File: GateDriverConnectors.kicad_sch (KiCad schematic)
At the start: 4 parts, among them J10 PWR/SIG_L1, J12 PWR/SIG_L1, J13 PWR/SIG_H1, J14 GateDriverConn1

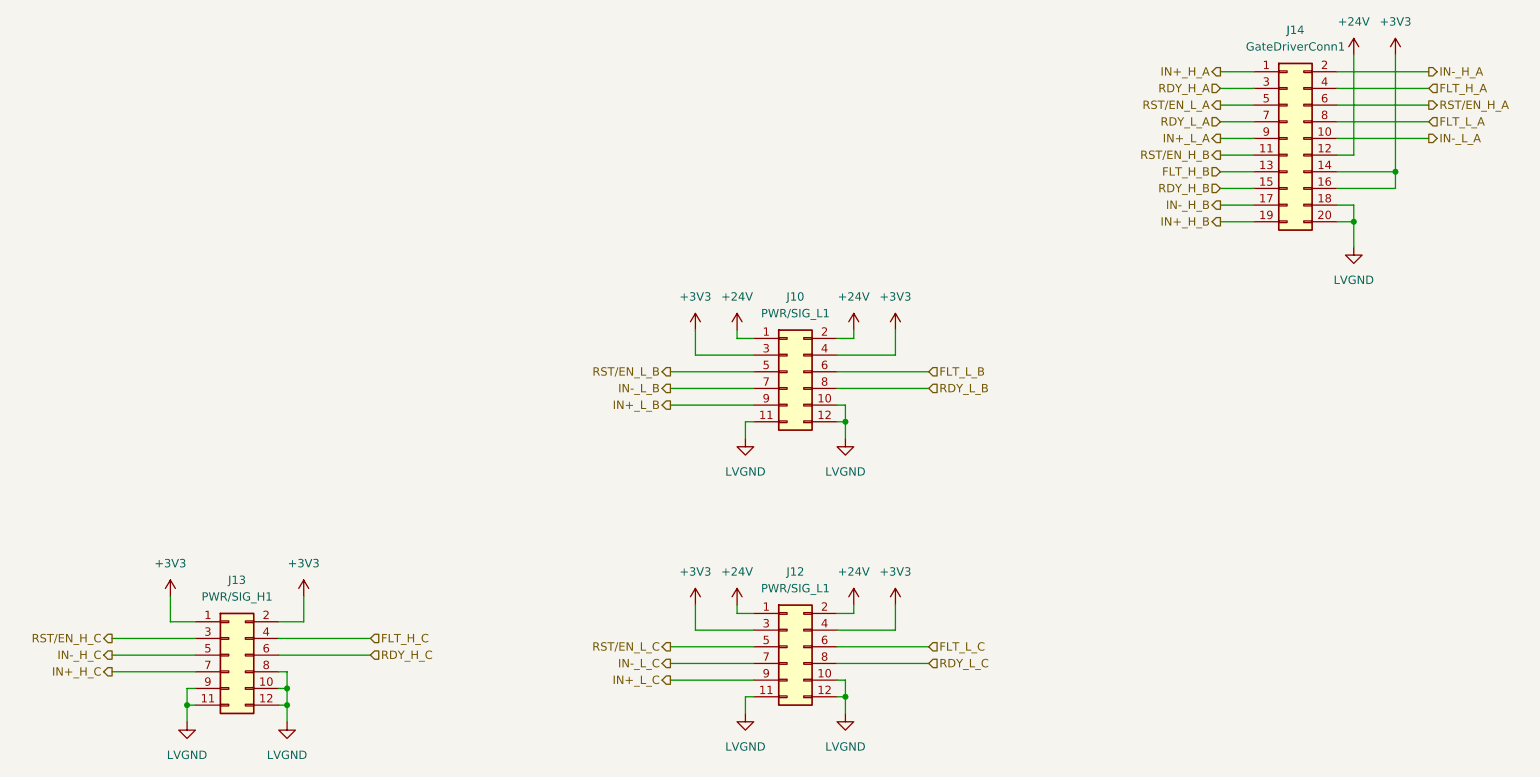
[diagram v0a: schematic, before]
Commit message: gate driver connector 2
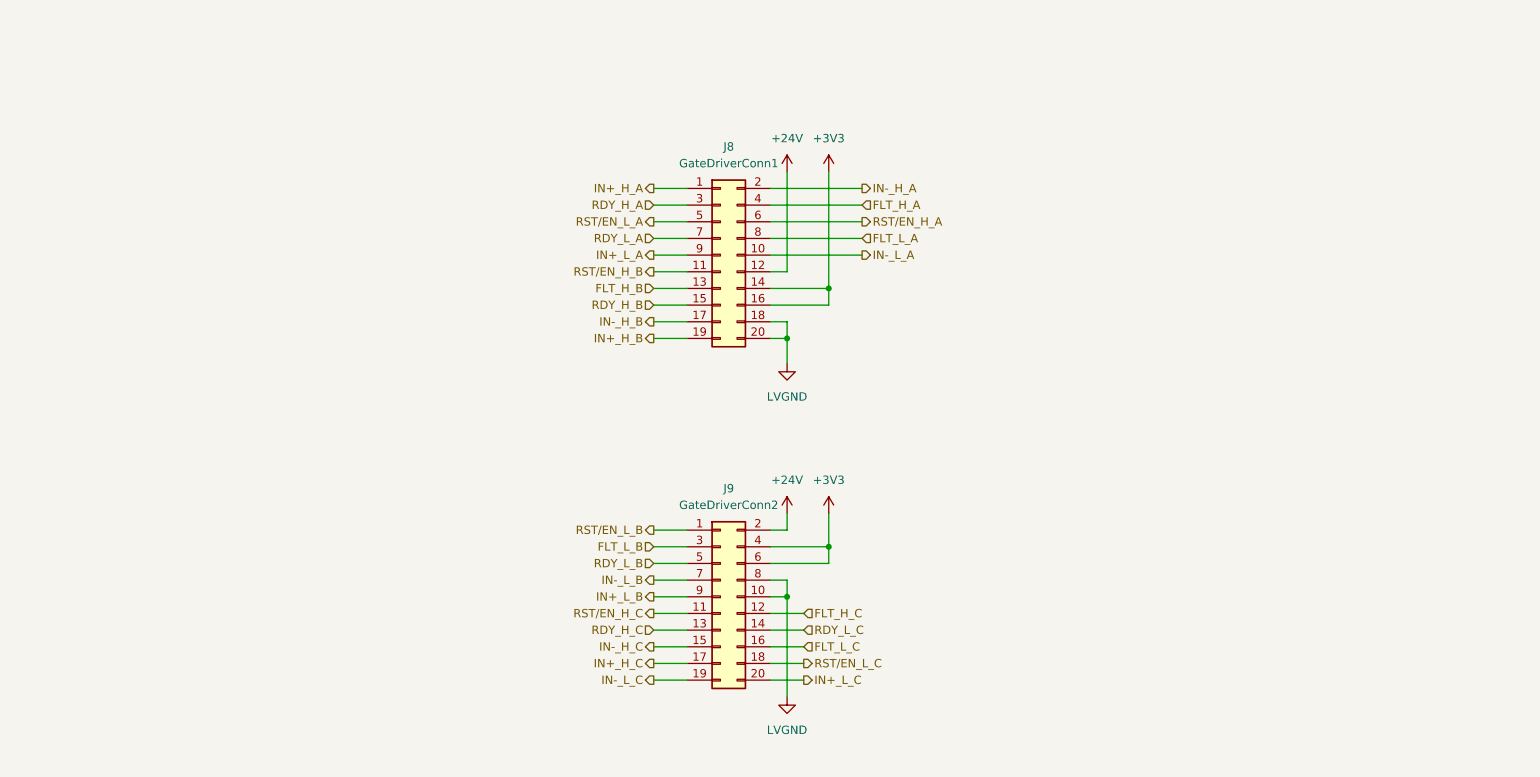
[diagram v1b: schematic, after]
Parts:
- removed J10, J12: PWR/SIG_L1, Connector_PinHeader_2.54mm:PinHeader_2x06_P2.54mm_Vertical, symbol Connector_Generic:Conn_02x06_Odd_Even
- removed J13: PWR/SIG_H1, Connector_PinHeader_2.54mm:PinHeader_2x06_P2.54mm_Vertical, symbol Connector_Generic:Conn_02x06_Odd_Even
- added J9: GateDriverConn2, Connector_PinHeader_2.54mm:PinHeader_2x10_P2.54mm_Vertical, symbol Connector_Generic:Conn_02x10_Odd_Even
- renumbered J14 to J8
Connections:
- net +24V: now also J9.2 (Pin_2)
- net +3V3: now also J9.4 (Pin_4), J9.6 (Pin_6)
- net FLT_H_C: now also J9.12 (Pin_12)
- net FLT_L_B: now also J9.3 (Pin_3)
- net FLT_L_C: now also J9.16 (Pin_16)
- net IN+_H_C: now also J9.17 (Pin_17)
- net IN+_L_B: now also J9.9 (Pin_9)
- net IN+_L_C: now also J9.20 (Pin_20)
- net IN-_H_C: now also J9.15 (Pin_15)
- net IN-_L_B: now also J9.7 (Pin_7)
- net IN-_L_C: now also J9.19 (Pin_19)
- net LVGND: now also J9.10 (Pin_10), J9.8 (Pin_8)
- net RDY_H_C: now also J9.13 (Pin_13)
- net RDY_L_B: now also J9.5 (Pin_5)
- net RDY_L_C: now also J9.14 (Pin_14)
- net RST/EN_H_C: now also J9.11 (Pin_11)
- net RST/EN_L_B: now also J9.1 (Pin_1)
- net RST/EN_L_C: now also J9.18 (Pin_18)
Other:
- moved on the sheet: J8
